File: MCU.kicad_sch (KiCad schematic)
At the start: 32 parts, among them J4 2125281600, J5 Conn_02x08_Odd_Even, J6 Conn_02x08_Odd_Even, U7 STM32F405RGTx, Y1 8MHz

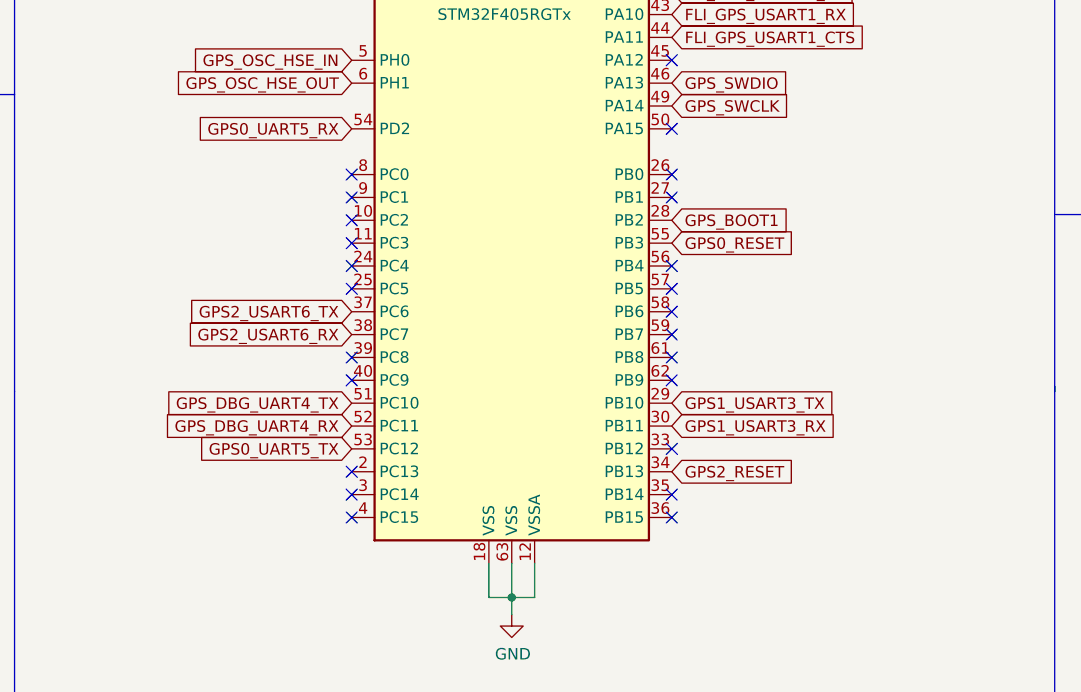
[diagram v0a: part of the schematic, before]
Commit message: Adding RF
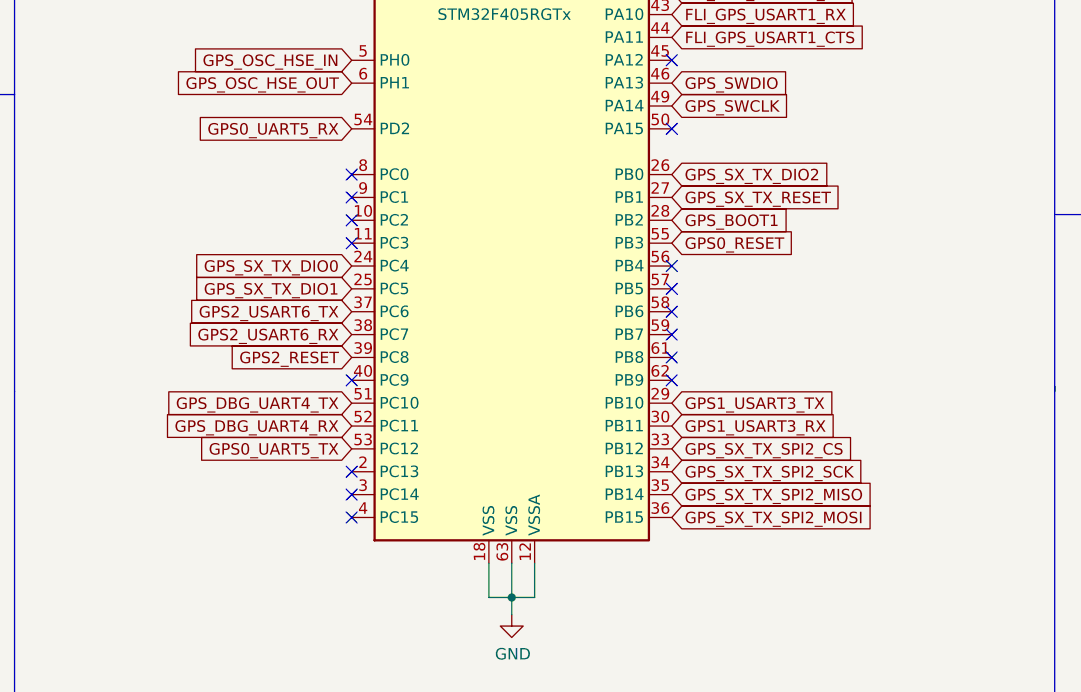
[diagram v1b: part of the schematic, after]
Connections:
- net GPS2_RESET: now also U7.39 (PC8); no longer U7.34 (PB13)
- net GPS_SX_TX_DIO0: now reaches U7.24 (PC4)
- net GPS_SX_TX_DIO1: now reaches U7.25 (PC5)
- net GPS_SX_TX_DIO2: now reaches U7.26 (PB0)
- net GPS_SX_TX_RESET: now reaches U7.27 (PB1)
- net GPS_SX_TX_SPI2_CS: now reaches U7.33 (PB12)
- net GPS_SX_TX_SPI2_MISO: now reaches U7.35 (PB14)
- net GPS_SX_TX_SPI2_MOSI: now reaches U7.36 (PB15)
- new net GPS_SX_TX_SPI2_SCK: U7.34 (PB13)
- no-connect marks 36 -> 28
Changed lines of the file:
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@@
   )
   (no_connect (at 139.7 134.62))
-  (no_connect (at 139.7 124.46))
   (no_connect (at 139.7 111.76))
   (no_connect (at 219.71 95.25))
@@
   (no_connect (at 104.14 162.56))
   (no_connect (at 245.11 92.71))
-  (no_connect (at 139.7 162.56))
   (no_connect (at 139.7 144.78))
   (no_connect (at 139.7 93.98))
   (no_connect (at 104.14 160.02))
   (no_connect (at 139.7 142.24))
-  (no_connect (at 139.7 127))
   (no_connect (at 219.71 97.79))
   (no_connect (at 104.14 147.32))
@@
   (no_connect (at 139.7 137.16))
   (no_connect (at 139.7 119.38))
-  (no_connect (at 104.14 134.62))
   (no_connect (at 245.11 100.33))
   (no_connect (at 104.14 127))
@@
   (no_connect (at 139.7 81.28))
   (no_connect (at 219.71 100.33))
-  (no_connect (at 139.7 154.94))
-  (no_connect (at 139.7 160.02))
   (no_connect (at 245.11 95.25))
   (no_connect (at 139.7 96.52))
-  (no_connect (at 104.14 137.16))
-  (no_connect (at 104.14 144.78))
   (no_connect (at 104.14 124.46))
   (wire (pts (xy 119.38 72.39) (xy 119.38 76.2))
@@
     )
   )
+  (global_label "GPS_SX_TX_DIO2" (shape input) (at 139.7 124.46 0) (fields_autoplaced)
+    (effects (font (size 1.27 1.27)) (justify left))
+    (property "Intersheet References" "${INTERSHEET_REFS}" (id 0) (at 157.7764 124.5394 0)
+      (effects (font (size 1.27 1.27)) (justify left) hide)
+    )
+  )
   (global_label "FLI_GPS_USART1_TX" (shape input) (at 223.393 162.306 180) (fields_autoplaced)
     (effects (font (size 1.27 1.27)) (justify right))
@@
     )
   )
+  (global_label "GPS_SX_TX_SPI2_SCK" (shape input) (at 139.7 157.48 0) (fields_autoplaced)
+    (effects (font (size 1.27 1.27)) (justify left))
+    (property "Intersheet References" "${INTERSHEET_REFS}" (id 0) (at 162.3726 157.5594 0)
+      (effects (font (size 1.27 1.27)) (justify left) hide)
+    )
+  )
   (global_label "GPS_DBG_UART4_TX" (shape input) (at 104.14 149.86 180) (fields_autoplaced)
     (effects (font (size 1.27 1.27)) (justify right))
@@
     )
   )
-  (global_label "GPS2_RESET" (shape input) (at 139.7 157.48 0) (fields_autoplaced)
-    (effects (font (size 1.27 1.27)) (justify left))
-    (property "Intersheet References" "${INTERSHEET_REFS}" (id 0) (at 153.785 157.4006 0)
-      (effects (font (size 1.27 1.27)) (justify left) hide)
+  (global_label "GPS2_RESET" (shape input) (at 104.14 144.78 180) (fields_autoplaced)
+    (effects (font (size 1.27 1.27)) (justify right))
+    (property "Intersheet References" "${INTERSHEET_REFS}" (id 0) (at 90.055 144.8594 0)
+      (effects (font (size 1.27 1.27)) (justify right) hide)
     )
   )
@@
     )
   )
+  (global_label "GPS_SX_TX_SPI2_MOSI" (shape input) (at 139.7 162.56 0) (fields_autoplaced)
+    (effects (font (size 1.27 1.27)) (justify left))
+    (property "Intersheet References" "${INTERSHEET_REFS}" (id 0) (at 163.2193 162.6394 0)
+      (effects (font (size 1.27 1.27)) (justify left) hide)
+    )
+  )
   (global_label "GPS2_USART6_TX" (shape input) (at 104.14 139.7 180) (fields_autoplaced)
     (effects (font (size 1.27 1.27)) (justify right))
@@
     )
   )
+  (global_label "GPS_SX_TX_DIO0" (shape input) (at 104.14 134.62 180) (fields_autoplaced)
+    (effects (font (size 1.27 1.27)) (justify right))
+    (property "Intersheet References" "${INTERSHEET_REFS}" (id 0) (at 86.0636 134.5406 0)
+      (effects (font (size 1.27 1.27)) (justify right) hide)
+    )
+  )
   (global_label "GPS1_USART3_TX" (shape input) (at 139.7 149.86 0) (fields_autoplaced)
     (effects (font (size 1.27 1.27)) (justify left))
@@
     )
   )
+  (global_label "GPS_SX_TX_SPI2_CS" (shape input) (at 139.7 154.94 0) (fields_autoplaced)
+    (effects (font (size 1.27 1.27)) (justify left))
+    (property "Intersheet References" "${INTERSHEET_REFS}" (id 0) (at 161.1026 155.0194 0)
+      (effects (font (size 1.27 1.27)) (justify left) hide)
+    )
+  )
   (global_label "GPS_BOOT1" (shape input) (at 139.7 129.54 0) (fields_autoplaced)
     (effects (font (size 1.27 1.27)) (justify left))
@@
     )
   )
+  (global_label "GPS_SX_TX_DIO1" (shape input) (at 104.14 137.16 180) (fields_autoplaced)
+    (effects (font (size 1.27 1.27)) (justify right))
+    (property "Intersheet References" "${INTERSHEET_REFS}" (id 0) (at 86.0636 137.0806 0)
+      (effects (font (size 1.27 1.27)) (justify right) hide)
+    )
+  )
   (global_label "GPS_DBG_UART4_RX" (shape input) (at 104.14 152.4 180) (fields_autoplaced)
     (effects (font (size 1.27 1.27)) (justify right))
@@
     )
   )
+  (global_label "GPS_SX_TX_RESET" (shape input) (at 139.7 127 0) (fields_autoplaced)
+    (effects (font (size 1.27 1.27)) (justify left))
+    (property "Intersheet References" "${INTERSHEET_REFS}" (id 0) (at 159.1069 127.0794 0)
+      (effects (font (size 1.27 1.27)) (justify left) hide)
+    )
+  )
+  (global_label "GPS_SX_TX_SPI2_MISO" (shape input) (at 139.7 160.02 0) (fields_autoplaced)
+    (effects (font (size 1.27 1.27)) (justify left))
+    (property "Intersheet References" "${INTERSHEET_REFS}" (id 0) (at 163.2193 160.0994 0)
+      (effects (font (size 1.27 1.27)) (justify left) hide)
+    )
+  )
